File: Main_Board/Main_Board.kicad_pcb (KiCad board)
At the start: 4 copper layers, 120 x 140 mm, 83 parts, among them J1 Conn_01x06, J10 HR-SR04_L_CONN, J11 12V_OUT, J12 BATT_REG_IN, J13 LED_CONN, J14 PD_CONN, J2 Conn_01x06, J3 Conn_01x06, J4 BATT_IN, J5 Conn_02x08_Top_Bottom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

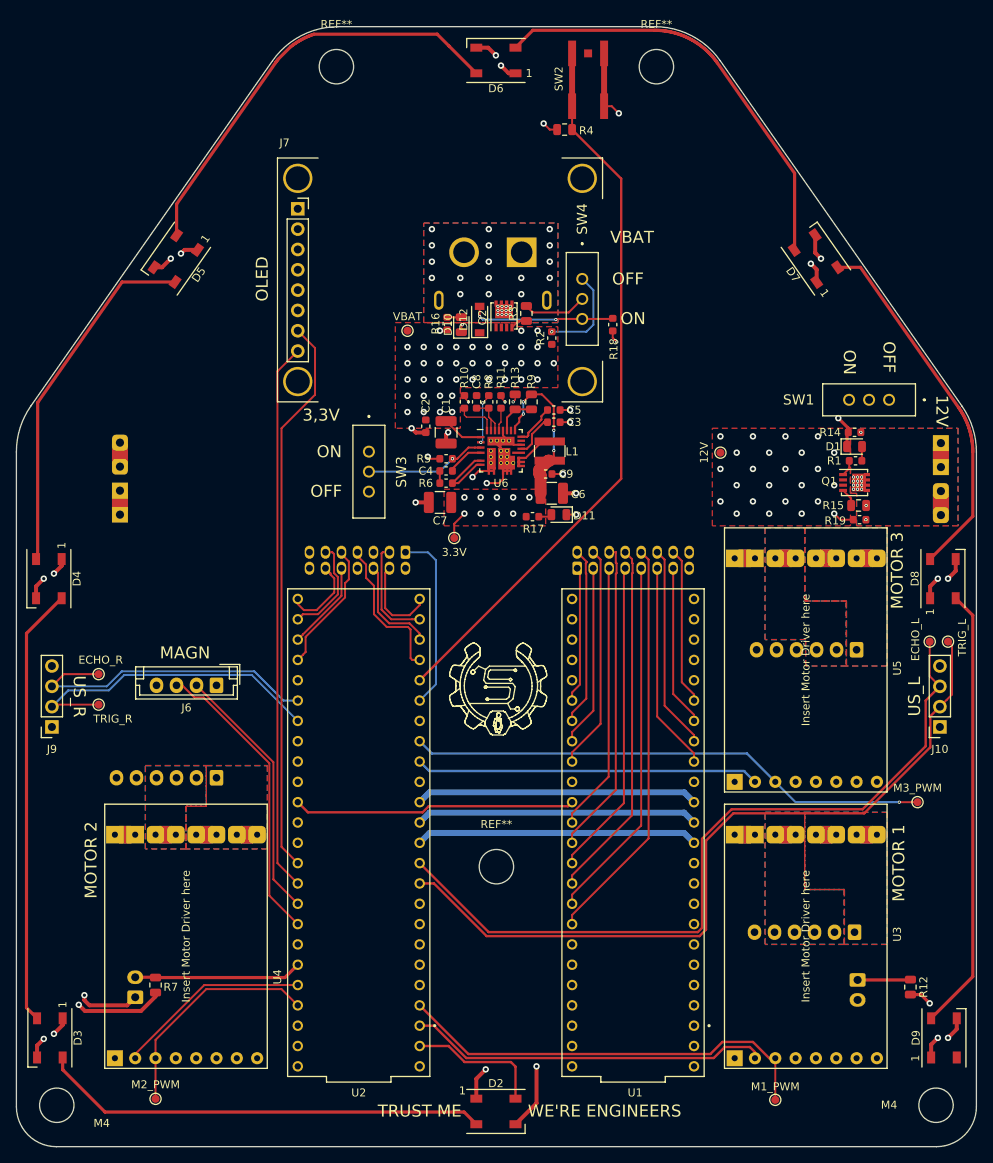
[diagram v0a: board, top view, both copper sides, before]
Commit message: Progress with pcb [IR BOARD]
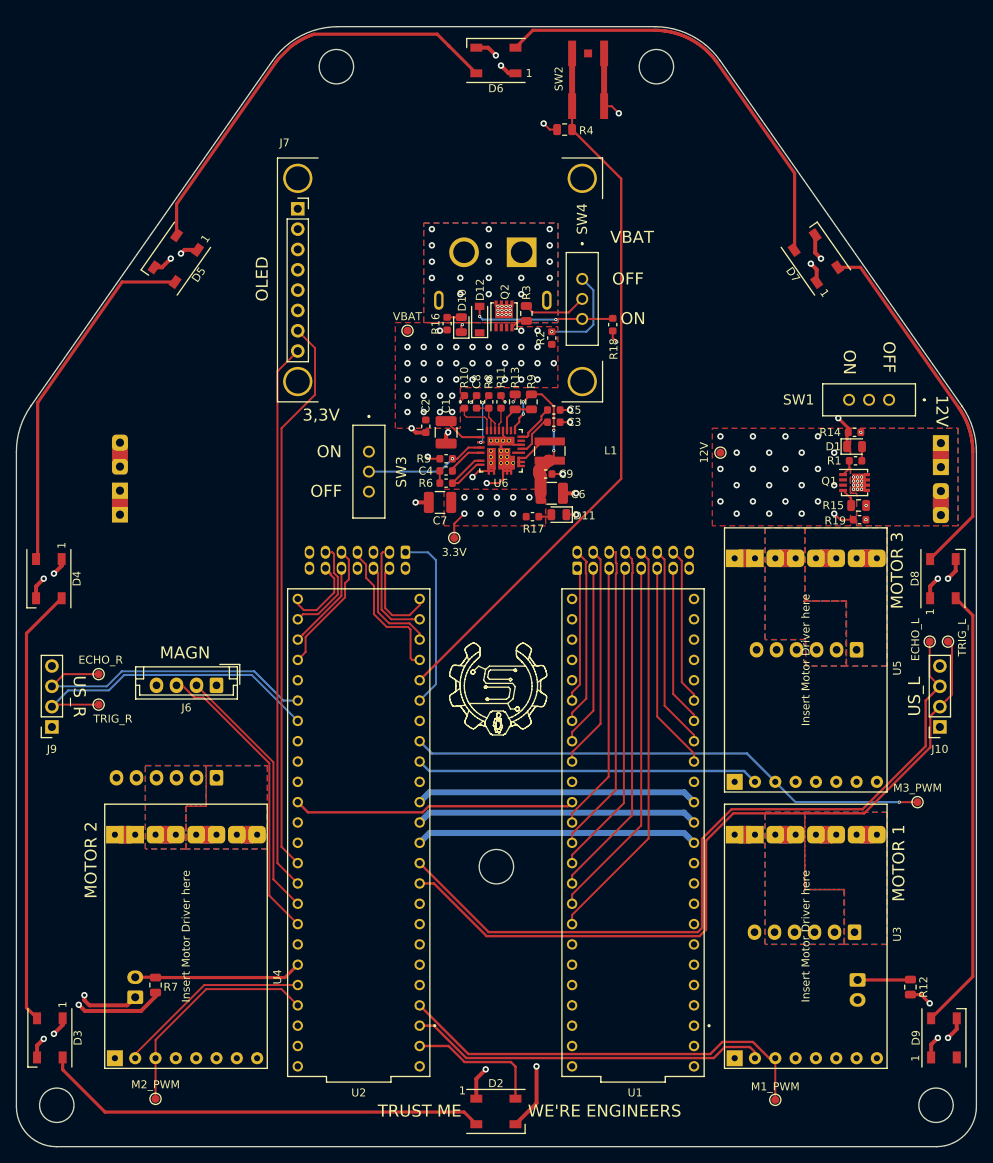
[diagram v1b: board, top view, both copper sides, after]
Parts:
- R1: value 120R -> 234R
- R12: value 10k -> 20R
- R16: value 120R -> 520R
- R17: value 120R -> 70R
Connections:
- D9 pad 2: Net-(D9-Pad2) -> unconnected-(D9-Pad2)
- J1 pad 3: Net-(J1-Pad3) -> unconnected-(J1-Pad3)
- J1 pad 4: Net-(J1-Pad4) -> unconnected-(J1-Pad4)
- J1 pad 5: Net-(J1-Pad5) -> unconnected-(J1-Pad5)
- J1 pad 6: Net-(J1-Pad6) -> unconnected-(J1-Pad6)
- J2 pad 3: Net-(J2-Pad3) -> unconnected-(J2-Pad3)
- J2 pad 4: Net-(J2-Pad4) -> unconnected-(J2-Pad4)
- J2 pad 5: Net-(J2-Pad5) -> unconnected-(J2-Pad5)
- J2 pad 6: Net-(J2-Pad6) -> unconnected-(J2-Pad6)
- J3 pad 3: Net-(J3-Pad3) -> unconnected-(J3-Pad3)
- J3 pad 4: Net-(J3-Pad4) -> unconnected-(J3-Pad4)
- J3 pad 5: Net-(J3-Pad5) -> unconnected-(J3-Pad5)
- J3 pad 6: Net-(J3-Pad6) -> unconnected-(J3-Pad6)
- J4 pad 1: Net-(J4-Pad2) -> GND
- J4 pad 2: GND -> Net-(J4-Pad2)
- J7 pad 3: Net-(J7-Pad3) -> unconnected-(J7-Pad3)
- J7 pad 4: Net-(J7-Pad4) -> unconnected-(J7-Pad4)
- J7 pad 5: Net-(J7-Pad5) -> unconnected-(J7-Pad5)
- J7 pad 6: Net-(J7-Pad6) -> unconnected-(J7-Pad6)
- U1 pad 0: Net-(U1-Pad0) -> unconnected-(U1-Pad0)
- U1 pad 1: Net-(U1-Pad1) -> unconnected-(U1-Pad1)
- U1 pad 2: Net-(U1-Pad2) -> unconnected-(U1-Pad2)
- U1 pad 20: Net-(U1-Pad20) -> unconnected-(U1-Pad20)
- U1 pad 21: Net-(U1-Pad21) -> unconnected-(U1-Pad21)
- U1 pad 22: Net-(U1-Pad22) -> unconnected-(U1-Pad22)
- U1 pad 23: Net-(U1-Pad23) -> unconnected-(U1-Pad23)
- U1 pad 28: Net-(U1-Pad28) -> unconnected-(U1-Pad28)
- U1 pad 29: Net-(U1-Pad29) -> unconnected-(U1-Pad29)
- U1 pad 3: Net-(U1-Pad3) -> unconnected-(U1-Pad3)
- U1 pad 3.3V_2: Net-(U1-Pad3.3V_1) -> (no net)
- U1 pad 30: Net-(U1-Pad30) -> unconnected-(U1-Pad30)
- U1 pad 31: Net-(U1-Pad31) -> unconnected-(U1-Pad31)
- U1 pad 32: Net-(U1-Pad32) -> unconnected-(U1-Pad32)
- U1 pad 33: Net-(U1-Pad33) -> unconnected-(U1-Pad33)
- U1 pad 34: Net-(U1-Pad34) -> unconnected-(U1-Pad34)
- U1 pad 35: Net-(U1-Pad35) -> unconnected-(U1-Pad35)
- U1 pad 36: Net-(U1-Pad36) -> unconnected-(U1-Pad36)
- U1 pad 37: Net-(U1-Pad37) -> unconnected-(U1-Pad37)
- U1 pad 4: Net-(U1-Pad4) -> unconnected-(U1-Pad4)
- U1 pad 5: Net-(U1-Pad5) -> unconnected-(U1-Pad5)
- U1 pad 6: Net-(U1-Pad6) -> unconnected-(U1-Pad6)
- U1 pad 7: Net-(U1-Pad7) -> unconnected-(U1-Pad7)
- U1 pad 8: Net-(U1-Pad8) -> unconnected-(U1-Pad8)
- U1 pad 9: Net-(U1-Pad9) -> unconnected-(U1-Pad9)
- U2 pad 14: Net-(U2-Pad14) -> unconnected-(U2-Pad14)
- U2 pad 15: Net-(U2-Pad15) -> unconnected-(U2-Pad15)
- U2 pad 20: Net-(U2-Pad20) -> unconnected-(U2-Pad20)
- U2 pad 26: Net-(U2-Pad26) -> unconnected-(U2-Pad26)
- U2 pad 3: Net-(U2-Pad3) -> unconnected-(U2-Pad3)
- U2 pad 3.3V_2: Net-(U2-Pad3.3V_1) -> (no net)
- U2 pad 37: Net-(U2-Pad37) -> unconnected-(U2-Pad37)
- U2 pad 4: Net-(U2-Pad4) -> unconnected-(U2-Pad4)
- U2 pad 40: Net-(U2-Pad40) -> unconnected-(U2-Pad40)
- U2 pad 41: Net-(U2-Pad41) -> unconnected-(U2-Pad41)
- U2 pad 5: Net-(U2-Pad5) -> unconnected-(U2-Pad5)
- U2 pad 6: Net-(U2-Pad6) -> unconnected-(U2-Pad6)
- U2 pad 7: Net-(U2-Pad7) -> unconnected-(U2-Pad7)
- U3 pad 10: Net-(U3-Pad10) -> unconnected-(U3-Pad10)
- U3 pad 11: Net-(U3-Pad11) -> unconnected-(U3-Pad11)
- U3 pad 12: Net-(U3-Pad12) -> unconnected-(U3-Pad12)
- U3 pad 8: Net-(U3-Pad8) -> unconnected-(U3-Pad8)
- U3 pad 9: Net-(U3-Pad9) -> unconnected-(U3-Pad9)
- U4 pad 10: Net-(U4-Pad10) -> unconnected-(U4-Pad10)
- U4 pad 11: Net-(U4-Pad11) -> unconnected-(U4-Pad11)
- U4 pad 12: Net-(U4-Pad12) -> unconnected-(U4-Pad12)
- U4 pad 8: Net-(U4-Pad8) -> unconnected-(U4-Pad8)
- U4 pad 9: Net-(U4-Pad9) -> unconnected-(U4-Pad9)
- U5 pad 10: Net-(U5-Pad10) -> unconnected-(U5-Pad10)
- U5 pad 11: Net-(U5-Pad11) -> unconnected-(U5-Pad11)
- U5 pad 12: Net-(U5-Pad12) -> unconnected-(U5-Pad12)
- U5 pad 8: Net-(U5-Pad8) -> unconnected-(U5-Pad8)
- U5 pad 9: Net-(U5-Pad9) -> unconnected-(U5-Pad9)
- U6 pad 15: Net-(U6-Pad15) -> unconnected-(U6-Pad15)
- U6 pad 18: Net-(U6-Pad18) -> unconnected-(U6-Pad18)
- U6 pad 21: Net-(U6-Pad21) -> unconnected-(U6-Pad21)
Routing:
- net GND: track 94.3 -> 95.6 mm, vias 26 -> 27
- net P3: track 17.0 -> 16.5 mm

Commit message: Finished IR, generated gerbers, ordered designs
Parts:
- added REF**: KiCad-Logo2_5mm_SilkScreen, Symbol:KiCad-Logo2_5mm_SilkScreen, B.Cu at (192.5, 155.2)
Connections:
- J5 pad 1: IR1 -> IR5
- J5 pad 10: IR10 -> GND
- J5 pad 11: IR11 -> IR14
- J5 pad 12: IR12 -> IR9
- J5 pad 14: IR14 -> IR10
- J5 pad 15: +3V3 -> IR12
- J5 pad 16: GND -> IR11
- J5 pad 2: IR2 -> IR6
- J5 pad 3: IR3 -> IR4
- J5 pad 4: IR4 -> IR7
- J5 pad 5: IR5 -> IR3
- J5 pad 6: IR6 -> IR8
- J5 pad 7: IR7 -> IR2
- J5 pad 8: IR8 -> +3V3
- J5 pad 9: IR9 -> IR1
- U1 pad 14: IR5 -> IR3
- U1 pad 15: IR6 -> IR8
- U1 pad 16: IR7 -> IR2
- U1 pad 17: IR8 -> IR1
- U1 pad 19: IR10 -> IR14
- U1 pad 24: IR11 -> IR10
- U1 pad 25: IR12 -> IR13
- U1 pad 26: IR13 -> IR11
- U1 pad 27: IR14 -> IR12
- U1 pad 38: IR1 -> IR5
- U1 pad 39: IR2 -> IR6
- U1 pad 40: IR3 -> IR4
- U1 pad 41: IR4 -> IR7
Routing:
- net IR14: track 19.6 -> 50.0 mm
- net IR1: track 17.1 -> 45.6 mm
- net IR10: track 50.8 -> 28.0 mm
- net IR2: track 22.4 -> 40.5 mm
- net IR6: track 39.5 -> 23.2 mm
- net IR5: track 33.7 -> 18.1 mm
- net IR3: track 22.7 -> 36.0 mm
- net IR7: track 39.6 -> 28.1 mm
- net IR12: track 25.5 -> 19.0 mm
- net IR8: track 44.9 -> 40.0 mm
- net IR4: track 28.0 -> 23.2 mm
- net IR9: track 45.5 -> 49.4 mm
- net IR11: track 26.1 -> 22.9 mm
- net IR13: track 20.2 -> 23.1 mm
